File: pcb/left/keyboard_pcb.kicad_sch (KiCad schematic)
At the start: 46 parts, among them J1 TRRS, J2 Conn_01x04_Male, K0 KEYSW, K1 KEYSW, K10 KEYSW, K11 KEYSW, K12 KEYSW, K13 KEYSW, K14 KEYSW, K15 KEYSW, K2 KEYSW, K20 KEYSW, K21 KEYSW, K22 KEYSW, K23 KEYSW, K24 KEYSW, K25 KEYSW, K3 KEYSW, K30 KEYSW, K31 KEYSW, K32 KEYSW, K4 KEYSW, K5 KEYSW, SW1 SW_SPDT, SW2 SW_SPDT, U1 PCF8574TS/3, U2 Pico

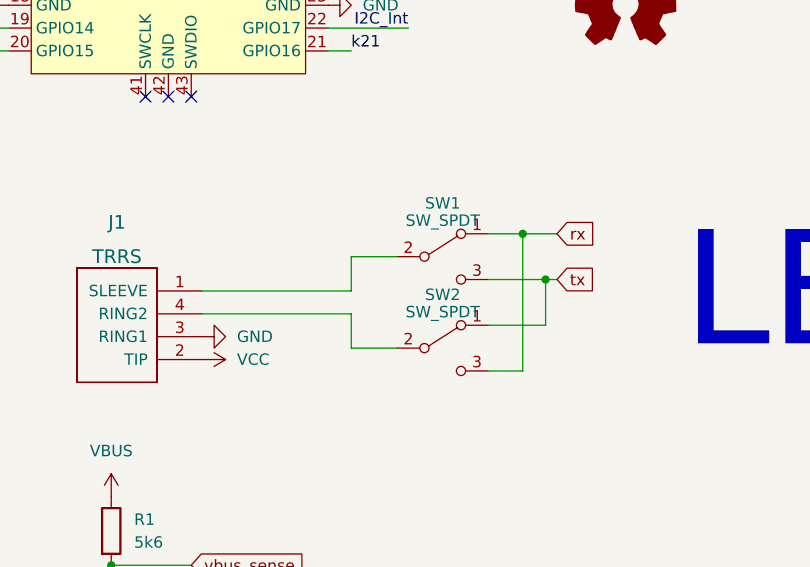
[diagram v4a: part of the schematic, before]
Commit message: Schematics are now Kicad 7 compatible
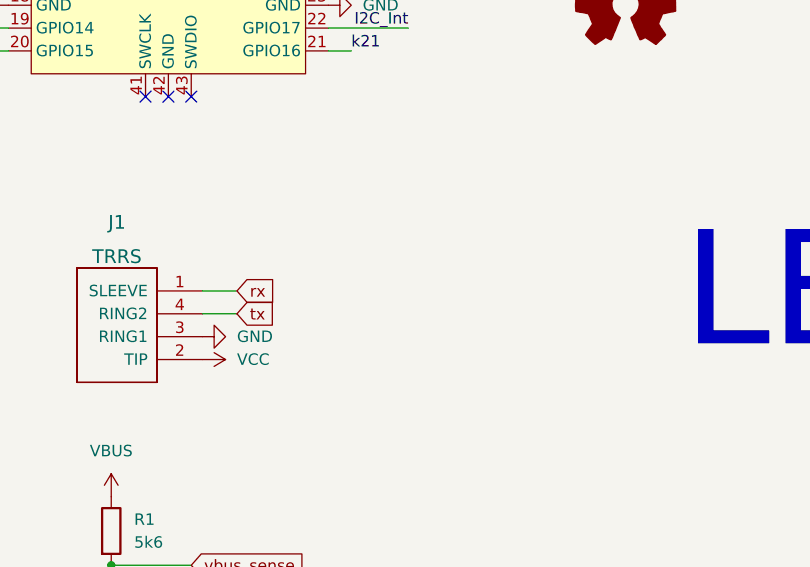
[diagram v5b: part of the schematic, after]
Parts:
- removed SW1, SW2: SW_SPDT, Jumper:SolderJumper-3_P1.3mm_Open_RoundedPad1.0x1.5mm_NumberLabels, symbol Switch:SW_SPDT
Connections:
- net rx: now also J1.1 (SLEEVE)
- net tx: now also J1.4 (RING2)
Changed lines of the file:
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@@
-(kicad_sch (version 20230221) (generator eeschema)
+(kicad_sch (version 20230121) (generator eeschema)
   (paper "A4")
   (title_block
     (rev "rev1.0")
   )
-  (junction (at 92.71 102.87) (diameter 0) (color 0 0 0 0)
-  )
   (junction (at 44.45 134.62) (diameter 0) (color 0 0 0 0)
   )
   (junction (at 185.42 149.86) (diameter 0) (color 0 0 0 0)
-  )
-  (junction (at 90.17 97.79) (diameter 0) (color 0 0 0 0)
   )
   (junction (at 193.04 139.7) (diameter 0) (color 0 0 0 0)
@@
     (stroke (width 0) (type default))
   )
-  (wire (pts (xy 86.36 97.79) (xy 90.17 97.79))
-    (stroke (width 0) (type default))
-  )
   (wire (pts (xy 251.46 30.48) (xy 256.54 30.48))
     (stroke (width 0) (type default))
@@
     (stroke (width 0) (type default))
   )
-  (wire (pts (xy 54.61 104.14) (xy 71.12 104.14))
-    (stroke (width 0) (type default))
-  )
   (wire (pts (xy 21.59 49.53) (xy 33.02 49.53))
     (stroke (width 0) (type default))
@@
     (stroke (width 0) (type default))
   )
-  (wire (pts (xy 54.61 106.68) (xy 71.12 106.68))
-    (stroke (width 0) (type default))
-  )
   (wire (pts (xy 21.59 74.93) (xy 33.02 74.93))
     (stroke (width 0) (type default))
   )
-  (wire (pts (xy 71.12 104.14) (xy 71.12 100.33))
-    (stroke (width 0) (type default))
-  )
   (wire (pts (xy 175.26 60.96) (xy 180.34 60.96))
     (stroke (width 0) (type default))
   )
-  (wire (pts (xy 71.12 106.68) (xy 71.12 110.49))
-    (stroke (width 0) (type default))
-  )
   (wire (pts (xy 251.46 60.96) (xy 256.54 60.96))
     (stroke (width 0) (type default))
@@
     (stroke (width 0) (type default))
   )
-  (wire (pts (xy 92.71 107.95) (xy 86.36 107.95))
-    (stroke (width 0) (type default))
-  )
-  (wire (pts (xy 90.17 97.79) (xy 93.98 97.79))
+  (wire (pts (xy 54.61 104.14) (xy 58.42 104.14))
     (stroke (width 0) (type default))
   )
@@
     (stroke (width 0) (type default))
   )
-  (wire (pts (xy 71.12 100.33) (xy 76.2 100.33))
-    (stroke (width 0) (type default))
-  )
   (wire (pts (xy 124.46 60.96) (xy 129.54 60.96))
     (stroke (width 0) (type default))
@@
     (stroke (width 0) (type default))
   )
-  (wire (pts (xy 92.71 102.87) (xy 92.71 107.95))
-    (stroke (width 0) (type default))
-  )
   (wire (pts (xy 21.59 69.85) (xy 33.02 69.85))
     (stroke (width 0) (type default))
@@
     (stroke (width 0) (type default))
   )
-  (wire (pts (xy 86.36 102.87) (xy 92.71 102.87))
-    (stroke (width 0) (type default))
-  )
   (wire (pts (xy 71.12 67.31) (xy 68.58 67.31))
     (stroke (width 0) (type default))
@@
     (stroke (width 0) (type default))
   )
-  (wire (pts (xy 90.17 97.79) (xy 90.17 113.03))
-    (stroke (width 0) (type default))
-  )
   (polyline (pts (xy 21.59 68.58) (xy 30.48 68.58))
     (stroke (width 0) (type default))
@@
     (stroke (width 0) (type default))
   )
-  (wire (pts (xy 92.71 102.87) (xy 93.98 102.87))
-    (stroke (width 0) (type default))
-  )
   (wire (pts (xy 68.58 69.85) (xy 71.12 69.85))
     (stroke (width 0) (type default))
   )
-  (wire (pts (xy 90.17 113.03) (xy 86.36 113.03))
-    (stroke (width 0) (type default))
-  )
   (wire (pts (xy 44.45 134.62) (xy 53.34 134.62))
     (stroke (width 0) (type default))
@@
     (stroke (width 0) (type default))
   )
-  (wire (pts (xy 71.12 110.49) (xy 76.2 110.49))
-    (stroke (width 0) (type default))
-  )
   (wire (pts (xy 27.94 54.61) (xy 33.02 54.61))
     (stroke (width 0) (type default))
@@
   )
   (wire (pts (xy 220.98 63.5) (xy 220.98 60.96))
+    (stroke (width 0) (type default))
+  )
+  (wire (pts (xy 54.61 106.68) (xy 58.42 106.68))
     (stroke (width 0) (type default))
   )
@@
     (effects (font (size 1.27 1.27)) (justify left bottom))
   )
-  (global_label "rx" (shape input) (at 93.98 97.79 0) (fields_autoplaced)
+  (global_label "rx" (shape input) (at 58.42 104.14 0) (fields_autoplaced)
     (effects (font (size 1.27 1.27)) (justify left))
-    (property "Intersheetrefs" "${INTERSHEET_REFS}" (at 98.2074 97.8694 0)
+    (property "Intersheetrefs" "${INTERSHEET_REFS}" (at 62.6474 104.2194 0)
       (effects (font (size 1.27 1.27)) (justify left) hide)
     )
@@
     )
   )
-  (global_label "tx" (shape input) (at 93.98 102.87 0) (fields_autoplaced)
+  (global_label "tx" (shape input) (at 58.42 106.68 0) (fields_autoplaced)
     (effects (font (size 1.27 1.27)) (justify left))
-    (property "Intersheetrefs" "${INTERSHEET_REFS}" (at 98.1469 102.9494 0)
+    (property "Intersheetrefs" "${INTERSHEET_REFS}" (at 62.5869 106.7594 0)
       (effects (font (size 1.27 1.27)) (justify left) hide)
     )
@@
         (path "/9538e4ed-27e6-4c37-b989-9859dc0d49e8"
           (reference "#PWR0137") (unit 1)
-        )
-      )
-    )
-  )
-  (symbol (lib_id "Switch:SW_SPDT") (at 81.28 100.33 0) (unit 1)
-    (in_bom yes) (on_board yes) (dnp no) (fields_autoplaced)
-    (property "Reference" "SW1" (at 81.28 94.3991 0)
-      (effects (font (size 1.27 1.27)))
-    )
-    (property "Value" "SW_SPDT" (at 81.28 96.3201 0)
-      (effects (font (size 1.27 1.27)))
-    )
-    (property "Footprint" "Jumper:SolderJumper-3_P1.3mm_Open_RoundedPad1.0x1.5mm_NumberLabels" (at 81.28 100.33 0)
-      (effects (font (size 1.27 1.27)) hide)
-    )
-    (property "Datasheet" "~" (at 81.28 100.33 0)
-      (effects (font (size 1.27 1.27)) hide)
-    )
-    (pin "1")
-    (pin "2")
-    (pin "3")
-    (instances
-      (project "keyboard_pcb"
-        (path "/9538e4ed-27e6-4c37-b989-9859dc0d49e8"
-          (reference "SW1") (unit 1)
         )
       )
@@
         )
       )
-    )
-  )
-  (symbol (lib_id "Switch:SW_SPDT") (at 81.28 110.49 0) (unit 1)
-    (in_bom yes) (on_board yes) (dnp no) (fields_autoplaced)
-    (property "Reference" "SW2" (at 81.28 104.5591 0)
-      (effects (font (size 1.27 1.27)))
-    )
-    (property "Value" "SW_SPDT" (at 81.28 106.4801 0)
-      (effects (font (size 1.27 1.27)))
-    )
-    (property "Footprint" "Jumper:SolderJumper-3_P1.3mm_Open_RoundedPad1.0x1.5mm_NumberLabels" (at 81.28 110.49 0)
-      (effects (font (size 1.27 1.27)) hide)
-    )
-    (property "Datasheet" "~" (at 81.28 110.49 0)
-      (effects (font (size 1.27 1.27)) hide)
-    )
-    (pin "1")
-    (pin "2")
-    (pin "3")
-    (instances
-      (project "keyboard_pcb"
-        (path "/9538e4ed-27e6-4c37-b989-9859dc0d49e8"
-          (reference "SW2") (unit 1)
-        )
-      )

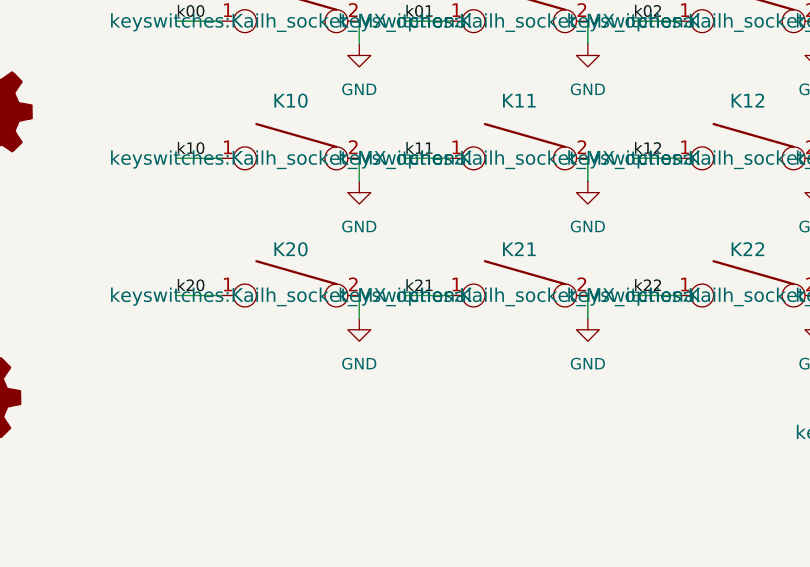
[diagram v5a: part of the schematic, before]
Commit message: finetuning regarding BOM and part placement
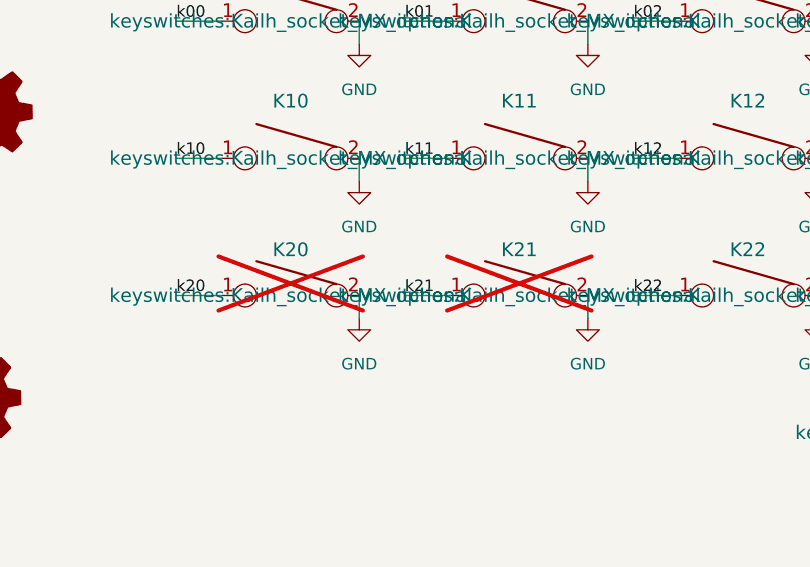
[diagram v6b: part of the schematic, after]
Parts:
- K20, K21: now not fitted; now left out of the parts list
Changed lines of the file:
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@@
   )
   (symbol (lib_id "keyboard_parts:KEYSW") (at 137.16 60.96 0) (mirror y) (unit 1)
-    (in_bom yes) (on_board yes) (dnp no)
+    (in_bom no) (on_board yes) (dnp yes)
     (property "Reference" "K20" (at 137.16 55.88 0)
       (effects (font (size 1.524 1.524)))
@@
   )
   (symbol (lib_id "keyboard_parts:KEYSW") (at 162.56 60.96 0) (mirror y) (unit 1)
-    (in_bom yes) (on_board yes) (dnp no)
+    (in_bom no) (on_board no) (dnp yes)
     (property "Reference" "K21" (at 162.56 55.88 0)
       (effects (font (size 1.524 1.524)))

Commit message: Revision 1.1 WIP#
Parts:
- removed J2: Conn_01x04_Male, Connector_PinHeader_2.54mm:PinHeader_1x04_P2.54mm_Vertical, symbol Connector:Conn_01x04_Male
- removed MB1, MB2, MB3, MB4: MountingHole, beekeeb_lib:mousebites, symbol Mechanical:MountingHole
- removed U1: PCF8574TS/3, Package_SO:SSOP-20_4.4x6.5mm_P0.65mm, symbol Interface_Expansion:PCF8574
- added H5, H6, H7, H8: MountingHole, misc:MountingHole_2.2mm_M2-8mm, symbol Mechanical:MountingHole
- added R10, R11, R12, R13, R14, R8, R9: 10k, Resistor_SMD:R_0603_1608Metric_Pad0.98x0.95mm_HandSolder, symbol Device:R
- added TP1: TestPoint, TestPoint:TestPoint_Pad_D3.0mm, symbol Connector:TestPoint
- added U1: MCP23009-E/SO, Package_SO:SOIC-18W_7.5x11.6mm_P1.27mm, symbol mcp23009:MCP23009-E/SO
- added U3: PCF8574TS, Package_SO:SSOP-20_4.4x6.5mm_P0.65mm, symbol Interface_Expansion:PCF8574TS
- H1, H2, H3, H4: footprint beekeeb_lib:MountingHole_2.2mm_M2-8mm -> misc:MountingHole_2.2mm_M2-8mm
- K0, K1, K10, K11, K12, K13, K14, K15, K2, K22, K23, K24, K25, K3, K30, K31, K32, K4, K5: footprint keyswitches:Kailh_socket_MX_optional_platemount -> keyswitches:Kailh_socket_MX_optional_platemount_3d_pretty_by_datasheet
- K20, K21: footprint keyswitches:Kailh_socket_MX_optional_platemount -> keyswitches:Kailh_socket_MX_optional_platemount_3d_pretty_by_datasheet; now fitted; now in the parts list
- R3, R4: value R -> 4k7; footprint Resistor_SMD:R_1206_3216Metric -> Resistor_SMD:R_0603_1608Metric_Pad0.98x0.95mm_HandSolder
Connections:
- net GND: now also U1.18 (VSS), U1.5 (ADR), U3.15 (VSS), U3.6 (A0), U3.7 (A1), U3.9 (A2)
- net I2C_Int: now also U1.7 (INT), U3.1 (~{INT})
- net LED_A: now also U1.14 (GP6), U3.19 (P6)
- net LED_B: now also U1.15 (GP7), U3.20 (P7)
- net SCL: now also U2.5 (GPIO3), U1.3 (SCL), U3.2 (SCL); no longer U2.15 (GPIO11)
- net SDA: now also U2.4 (GPIO2), U1.4 (SDA), U3.4 (SDA); no longer U2.14 (GPIO10)
- net VCC: no longer C1.1, C2.1, R3.1, R4.1, R5.1
- net k00: now also R10.2, U1.10 (GP2), U3.12 (P2)
- net k01: now also U2.29 (GPIO22); no longer U2.32 (GPIO27_ADC1)
- net k04: now also U2.31 (GPIO26_ADC0); no longer U2.5 (GPIO3)
- net k05: now also U2.32 (GPIO27_ADC1); no longer U2.4 (GPIO2)
- net k10: now also R9.2, U1.9 (GP1), U3.11 (P1)
- net k20: now also R8.2, U1.8 (GP0), U3.10 (P0)
- net k24: now also U2.27 (GPIO21); no longer U2.31 (GPIO26_ADC0)
- net k30: now also R13.2, U1.11 (GP3), U3.14 (P3)
- net k31: now also R12.2, U1.12 (GP4), U3.16 (P4)
- net k32: now also R11.2, U1.13 (GP5), U3.17 (P5)
- net +3.3V: now reaches U2.36 (3V3)
- net +3.3V: now also C1.1, C2.1, R3.1, R4.1, R5.1, R10.1, R11.1, R12.1, R13.1, R14.1, R8.1, R9.1, U1.1 (VDD), U3.5 (VDD)
- new net MCP_RST: R14.2, TP1.1, U1.6 (~{RESET})
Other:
- note added: "I2C1"
- note added: "left"
- note removed: "I2C to J2"
- moved on the sheet: C1, C2, D1, D2, H1, H2, H3, H4, R1, R2, R3, R4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

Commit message: Left side routing wip
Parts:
- removed U3: PCF8574TS, Package_SO:SSOP-20_4.4x6.5mm_P0.65mm, symbol Interface_Expansion:PCF8574TS
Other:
- moved on the sheet: R5, U1
